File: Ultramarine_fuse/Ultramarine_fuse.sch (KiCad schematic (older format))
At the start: 131 parts, among them J1 Conn_01x04_Female, J2 Conn_01x04_Female, J3 Conn_01x02_Female, SW1 SW_Push, SW10 SW_Push, SW11 SW_Push, SW12 SW_Push, SW13 SW_Push, SW14 SW_Push, SW15 SW_Push, SW16 SW_Push, SW17 SW_Push, SW18 SW_Push, SW19 SW_Push, SW2 SW_Push, SW20 SW_Push, SW21 SW_Push, SW22 SW_Push, SW23 SW_Push, SW24 SW_Push, SW25 SW_Push, SW26 SW_Push, SW27 SW_Push, SW28 SW_Push, SW29 SW_Push, SW3 SW_Push, SW30 SW_Push, SW31 SW_Push, SW32 SW_Push, SW33 SW_Push, SW34 SW_Push, SW35 SW_Push, SW36 SW_Push, SW4 SW_Push, SW5 SW_Push, SW6 SW_Push, SW7 SW_Push, SW8 SW_Push, SW9 SW_Push, U1 BLE-Micro-Pro, U10 SK6812mini, U11 SK6812mini, U12 SK6812mini, U13 SK6812mini, U14 SK6812mini, U15 SK6812mini, U16 SK6812mini, U17 SK6812mini, U18 SK6812mini, U19 SK6812mini, U2 SK6812mini, U20 SK6812mini, U21 SK6812mini, U22 SK6812mini, U23 SK6812mini, U24 SK6812mini, U25 SK6812mini, U26 SK6812mini, U27 SK6812mini, U28 SK6812mini, U29 SK6812mini, U3 SK6812mini, U30 SK6812mini, U31 SK6812mini, U32 SK6812mini, U33 SK6812mini, U34 SK6812mini, U35 SK6812mini, U36 SK6812mini, U37 TP4056, U4 SK6812mini, U5 SK6812mini, U6 SK6812mini, U7 SK6812mini, U8 SK6812mini, U9 SK6812mini

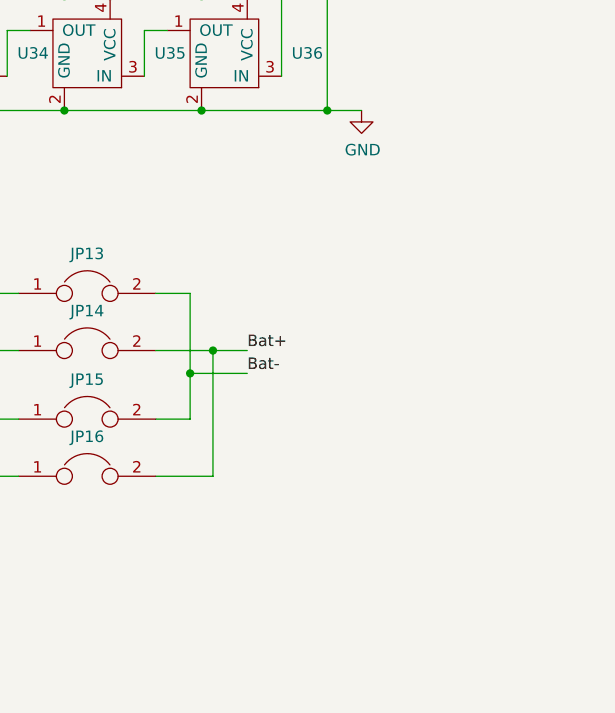
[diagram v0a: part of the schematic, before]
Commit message: add 3v3 regulator
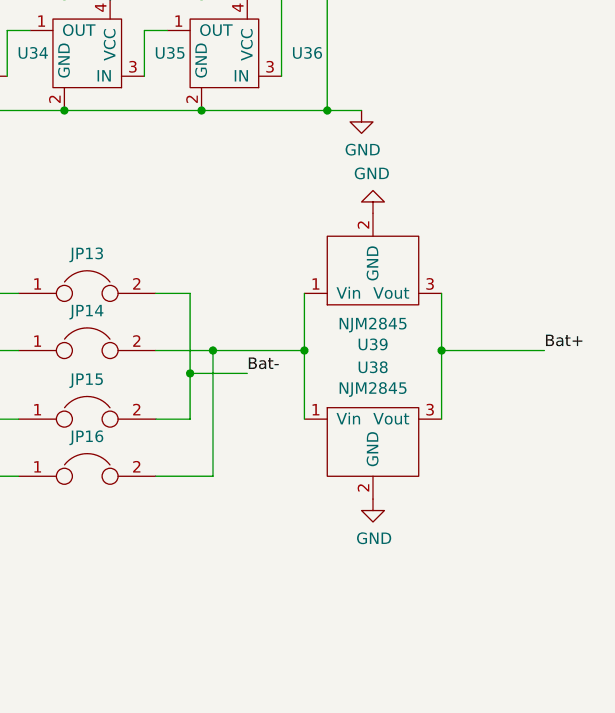
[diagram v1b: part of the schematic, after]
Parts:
- added U38, U39: NJM2845, Package_TO_SOT_SMD:TO-252-2, symbol Basic_SOP:NJM2845
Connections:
- net Bat+: now also U38.3 (Vout), U39.3 (Vout); no longer JP14.2, JP16.2
- net GND: now also U38.2 (GND), U39.2 (GND)
- new net: JP14.2, JP16.2, U38.1 (Vin), U39.1 (Vin)
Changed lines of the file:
@@
 	1    0    0    -1
 $EndComp
-Text Label 13350 4800 0    50   ~ 0
-Bat+
-Text Label 13350 4900 0    50   ~ 0
-Bat-
 $Comp
 L power:VCC #PWR0101
@@
 	10150 4550 10000 4550
 Wire Wire Line
-	13100 4900 13100 5100
-Wire Wire Line
-	13100 4900 13350 4900
-Wire Wire Line
-	13200 4800 13350 4800
-Connection ~ 13100 4900
-Wire Wire Line
-	13100 4550 13100 4900
-Wire Wire Line
 	13200 4800 13200 5350
 Wire Wire Line
 	13200 5350 12950 5350
-Connection ~ 13200 4800
 Wire Wire Line
 	12950 4800 13200 4800
@@
 Wire Wire Line
 	10250 5000 10250 5350
+Connection ~ 13200 4800
+Connection ~ 13100 4900
+Wire Wire Line
+	13100 4550 13100 4900
+Wire Wire Line
+	13100 4900 13100 5100
+Wire Wire Line
+	13100 4900 13350 4900
+Text Label 13350 4900 0    50   ~ 0
+Bat-
+Text Label 14650 4800 0    50   ~ 0
+Bat+
+$Comp
+L Basic_SOP:NJM2845 U38
+U 1 1 61CA94C5
+P 13900 5100
+F 0 "U38" H 13900 5325 50  0000 C CNN
+F 1 "NJM2845" H 13900 5234 50  0000 C CNN
+F 2 "Package_TO_SOT_SMD:TO-252-2" H 13900 5350 50  0001 C CNN
+F 3 "" H 13900 5350 50  0001 C CNN
+	1    13900 5100
+	1    0    0    -1
+$EndComp
+Wire Wire Line
+	13200 4800 13600 4800
+Wire Wire Line
+	14200 4800 14650 4800
+$Comp
+L power:GND #PWR0117
+U 1 1 61D2B088
+P 13900 5450
+F 0 "#PWR0117" H 13900 5200 50  0001 C CNN
+F 1 "GND" H 13905 5277 50  0000 C CNN
+F 2 "" H 13900 5450 50  0001 C CNN
+F 3 "" H 13900 5450 50  0001 C CNN
+	1    13900 5450
+	1    0    0    -1
+$EndComp
+$Comp
+L Basic_SOP:NJM2845 U39
+U 1 1 61D6CD6C
+P 13900 4550
+F 0 "U39" H 13900 4775 50  0000 C CNN
+F 1 "NJM2845" H 13900 4684 50  0000 C CNN
+F 2 "Package_TO_SOT_SMD:TO-252-2" H 13900 4800 50  0001 C CNN
+F 3 "" H 13900 4800 50  0001 C CNN
+	1    13900 4550
+	1    0    0    1
+$EndComp
+Wire Wire Line
+	13600 4550 13600 4800
+Connection ~ 13600 4800
+Wire Wire Line
+	13600 4800 13600 5100
+Wire Wire Line
+	14200 5100 14200 4800
+Connection ~ 14200 4800
+Wire Wire Line
+	14200 4800 14200 4550
+$Comp
+L power:GND #PWR0118
+U 1 1 61E4A740
+P 13900 4200
+F 0 "#PWR0118" H 13900 3950 50  0001 C CNN
+F 1 "GND" H 13905 4027 50  0000 C CNN
+F 2 "" H 13900 4200 50  0001 C CNN
+F 3 "" H 13900 4200 50  0001 C CNN
+	1    13900 4200
+	-1   0    0    1
+$EndComp
 $EndSCHEMATC
